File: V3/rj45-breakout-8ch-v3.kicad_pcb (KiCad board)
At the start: 2 copper layers, 93 x 67.8 mm, 13 parts, among them J1 Jack RJ45, J10 Conn_01x06, J11 Conn_01x06, J12 Conn_01x06, J13 Conn_01x06, J2 Jack RJ45, J3 Jack RJ45, J4 Jack RJ45, J5 Jack RJ45, J6 Jack RJ45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

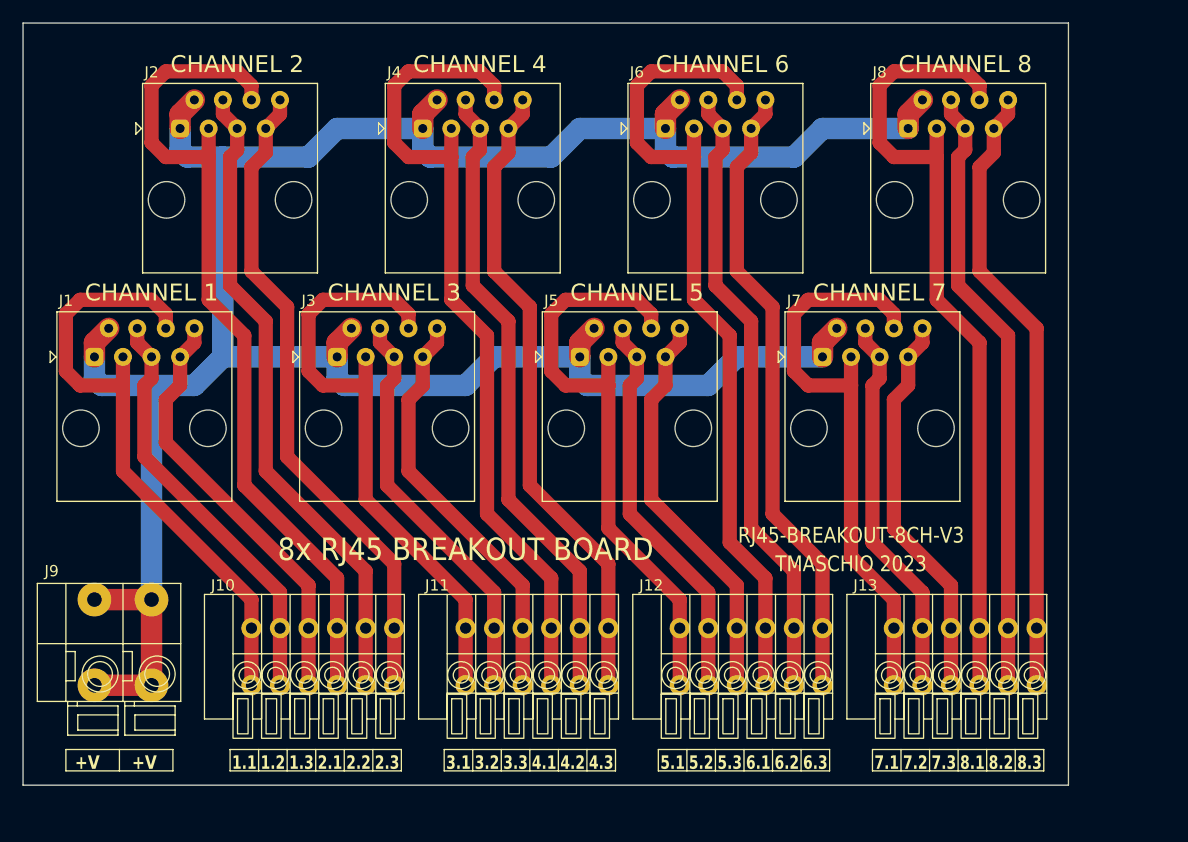
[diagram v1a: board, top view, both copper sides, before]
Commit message: Connectors rotated 180deg
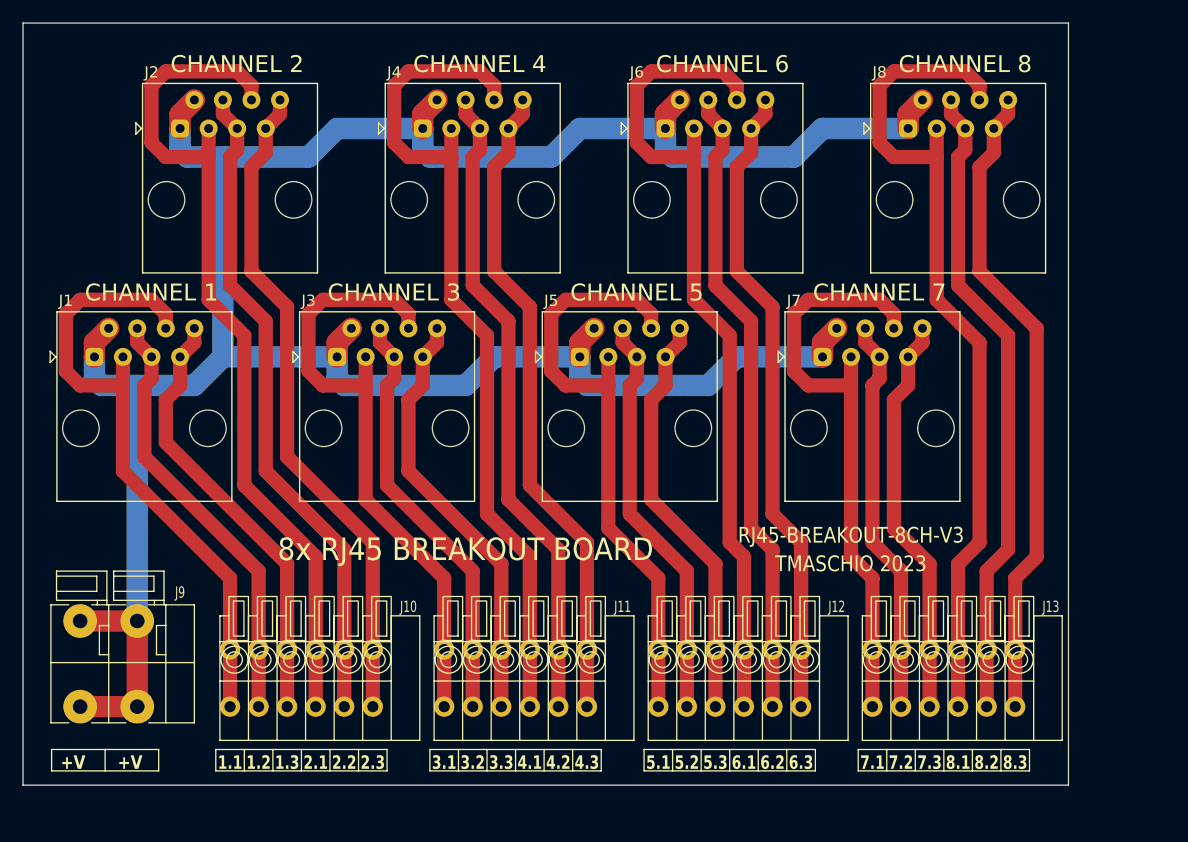
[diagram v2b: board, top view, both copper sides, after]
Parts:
- J10, J11, J12, J13: footprint Tales:TerminalBlock_DG141V-2.54-6P_1x06_P2.54mm_Vertical -> Tales:TerminalBlock_Phoenix_FFKDSA1-V-2.54-6_1x06_P2.54mm_Vertical
- J9: footprint Tales:TerminalBlock_JL142V-5.08-2P_1x02_P5.08mm_Vertical -> Tales:TerminalBlock_Phoenix_FFKDSA-V1-5.08-2_1x02_P5.08mm_Vertical
- moved J10 2.69 mm to (109.9, 120.0)
- moved J11 2.69 mm to (128.9, 120.0)
- moved J12 2.69 mm to (148.0, 120.0)
- moved J13 2.69 mm to (167.0, 120.0)
- moved J9 2.29 mm to (96.5, 120.0)
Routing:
- net Net-(J13-Pin_5): track 54.7 -> 57.4 mm
- net Net-(J13-Pin_4): track 73.0 -> 75.7 mm
- net Net-(J13-Pin_6): track 55.2 -> 57.9 mm
- net Net-(J9-Pin_1): track 228.0 -> 229.9 mm
- net Net-(J11-Pin_3): track 37.0 -> 38.1 mm
- net Net-(J10-Pin_4): track 76.2 -> 77.3 mm
- net Net-(J10-Pin_6): track 58.4 -> 59.5 mm
- net Net-(J13-Pin_3): track 34.9 -> 36.0 mm
- net Net-(J13-Pin_2): track 34.4 -> 35.5 mm
- net Net-(J12-Pin_6): track 56.3 -> 57.4 mm
- net Net-(J12-Pin_5): track 55.8 -> 56.9 mm
- net Net-(J12-Pin_4): track 74.1 -> 75.2 mm
- net Net-(J12-Pin_3): track 36.0 -> 37.1 mm
- net Net-(J12-Pin_1): track 53.7 -> 54.9 mm
- net Net-(J11-Pin_5): track 56.8 -> 57.9 mm
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
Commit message: Layout tweakings
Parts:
- added ?: , Tales:Grandmas_medium, F.Cu at (114.1, 103.8)
- J10: value Conn_01x06 -> SWITCHES1; footprint Tales:TerminalBlock_Phoenix_FFKDSA1-V-2.54-6_1x06_P2.54mm_Vertical -> Tales:TerminalBlock_DB141V-2.54-6P_1x06_P2.54mm_Vertical
- J11: value Conn_01x06 -> SWITCHES2; footprint Tales:TerminalBlock_Phoenix_FFKDSA1-V-2.54-6_1x06_P2.54mm_Vertical -> Tales:TerminalBlock_DB141V-2.54-6P_1x06_P2.54mm_Vertical
- J12: value Conn_01x06 -> SWITCHES3; footprint Tales:TerminalBlock_Phoenix_FFKDSA1-V-2.54-6_1x06_P2.54mm_Vertical -> Tales:TerminalBlock_DB141V-2.54-6P_1x06_P2.54mm_Vertical
- J13: value Conn_01x06 -> SWITCHES4; footprint Tales:TerminalBlock_Phoenix_FFKDSA1-V-2.54-6_1x06_P2.54mm_Vertical -> Tales:TerminalBlock_DB141V-2.54-6P_1x06_P2.54mm_Vertical
- J9: value Conn_01x02 -> 24V; footprint Tales:TerminalBlock_Phoenix_FFKDSA-V1-5.08-2_1x02_P5.08mm_Vertical -> Tales:TerminalBlock_DB142V-2-5.08_1x02_P5.08mm_Vertical
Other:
- board text added: "GHHA 2023"
- board text added: "Grandma's House"
- board text added: "Home Automation"
- board text removed: "8x RJ45 BREAKOUT BOARD"
- board text removed: "TMASCHIO 2023"

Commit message: Footprints updated
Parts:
- J1, J2, J3, J4, J5, J6, J7, J8: footprint Tales:RJ45_Amphenol_P-RJE08-188-0X10 -> Tales:RJ45_CKMTW_R-RJ45S08P-A004

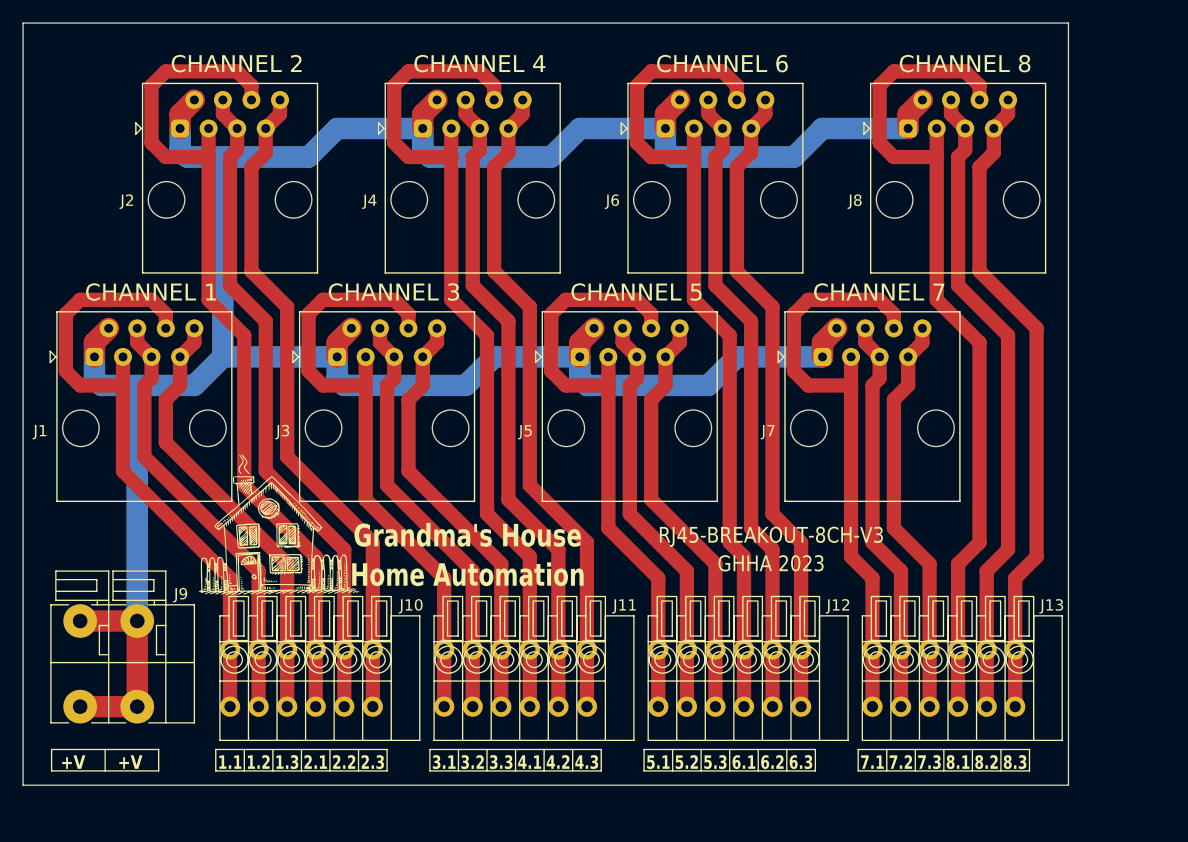
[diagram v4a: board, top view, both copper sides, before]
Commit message: Grid changed to mm
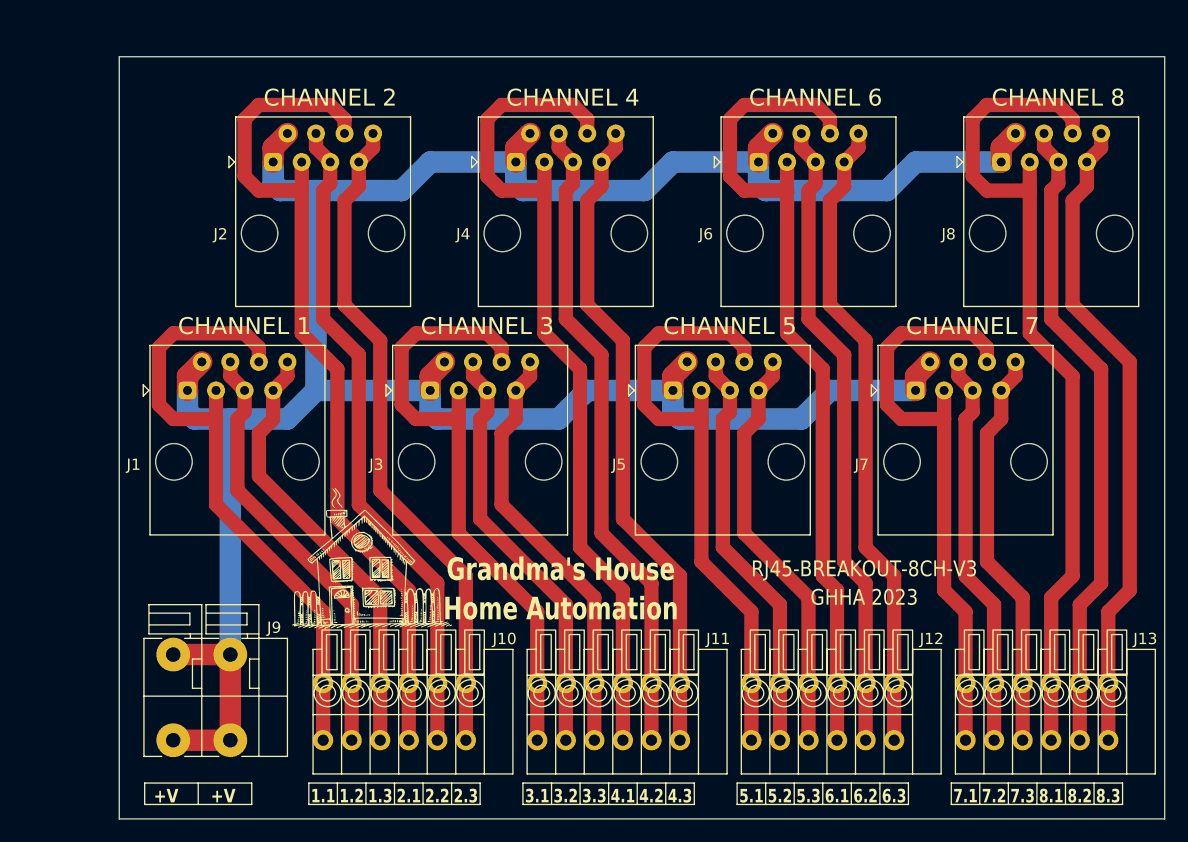
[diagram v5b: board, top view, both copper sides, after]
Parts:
- moved ? 8.80 mm to (122.4, 106.8)
- moved J1 8.80 mm to (110.5, 91.9)
- moved J10 8.80 mm to (118.1, 123.0)
- moved J11 8.80 mm to (137.2, 123.0)
- moved J12 8.80 mm to (156.2, 123.0)
- moved J13 8.80 mm to (175.3, 123.0)
- moved J2 8.80 mm to (118.1, 71.6)
- moved J4 8.80 mm to (139.7, 71.6)
- moved J5 8.80 mm to (153.7, 91.9)
- moved J6 8.80 mm to (161.3, 71.6)
- moved J7 8.80 mm to (175.3, 91.9)
- moved J8 8.80 mm to (182.9, 71.6)
- moved J9 8.80 mm to (104.8, 123.0)
- moved J3 8.80 mm to (132.1, 91.9)

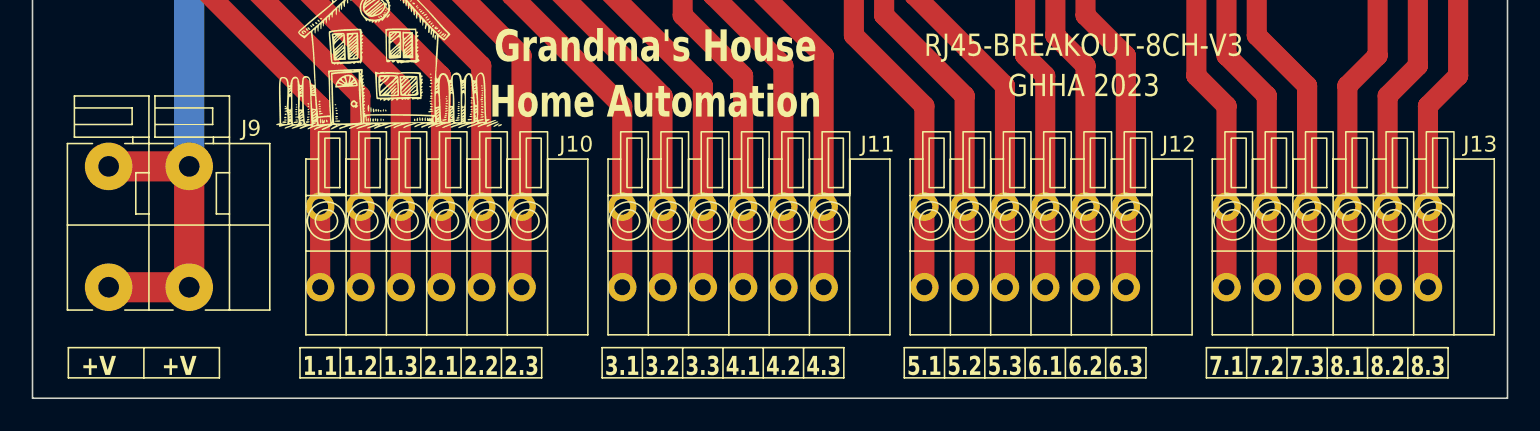
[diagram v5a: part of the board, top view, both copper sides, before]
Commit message: Align parts and tracks to mm grid
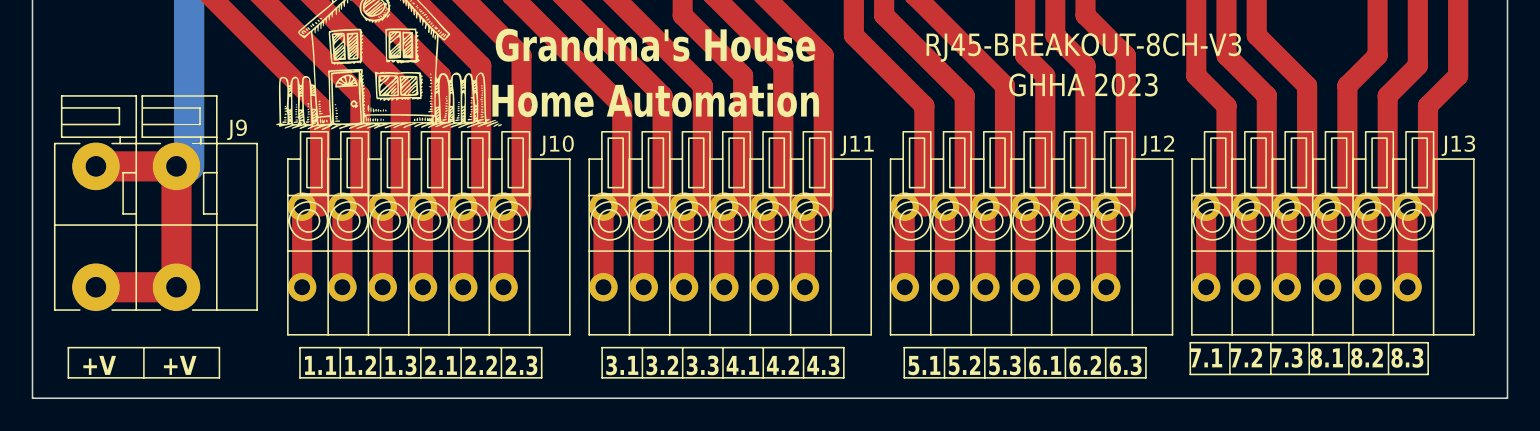
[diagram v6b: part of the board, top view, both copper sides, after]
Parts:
- moved J13 1.28 mm to (174.0, 123.0)
- moved J12 1.24 mm to (155.0, 123.0)
- moved J11 1.19 mm to (136.0, 123.0)
- moved J10 1.14 mm to (117.0, 123.0)
- moved J9 0.80 mm to (104.0, 123.0)

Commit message: Update rj45-breakout-8ch-v3.kicad_pcb
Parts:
- removed ?: , Tales:Grandmas_medium
- moved J7 0.36 mm to (174.9, 92.0)
- moved J2 0.32 mm to (118.4, 71.5)
- moved J5 0.28 mm to (153.4, 92.0)
- moved J4 0.23 mm to (139.9, 71.5)
- moved J3 0.20 mm to (131.9, 92.0)
- moved J6 0.15 mm to (161.4, 71.5)
- moved J1 0.13 mm to (110.4, 92.0)
- moved J8 0.08 mm to (182.9, 71.5)
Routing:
- net Net-(J12-Pin_2): track 36.5 -> 8.15 mm
- net Net-(J13-Pin_3): track 36.0 -> 8.15 mm
- net Net-(J13-Pin_2): track 35.5 -> 8.15 mm
- net Net-(J11-Pin_6): track 58.4 -> 38.2 mm
- net Net-(J13-Pin_6): track 57.9 -> 37.7 mm
- net Net-(J12-Pin_6): track 57.4 -> 38.2 mm
- net Net-(J11-Pin_5): track 57.9 -> 39.4 mm
- net Net-(J12-Pin_5): track 56.9 -> 39.4 mm
- net Net-(J11-Pin_4): track 76.2 -> 60.5 mm
- net Net-(J12-Pin_4): track 75.2 -> 60.5 mm
- net Net-(J12-Pin_3): track 37.1 -> 42.6 mm
- net Net-(J13-Pin_5): track 57.4 -> 55.6 mm
- net Net-(J9-Pin_1): track 229.9 -> 228.3 mm
- net Net-(J13-Pin_1): track 53.8 -> 55.4 mm
- net Net-(J13-Pin_4): track 75.7 -> 76.8 mm
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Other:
- board text removed: "Grandma's House"
- board text removed: "Home Automation"

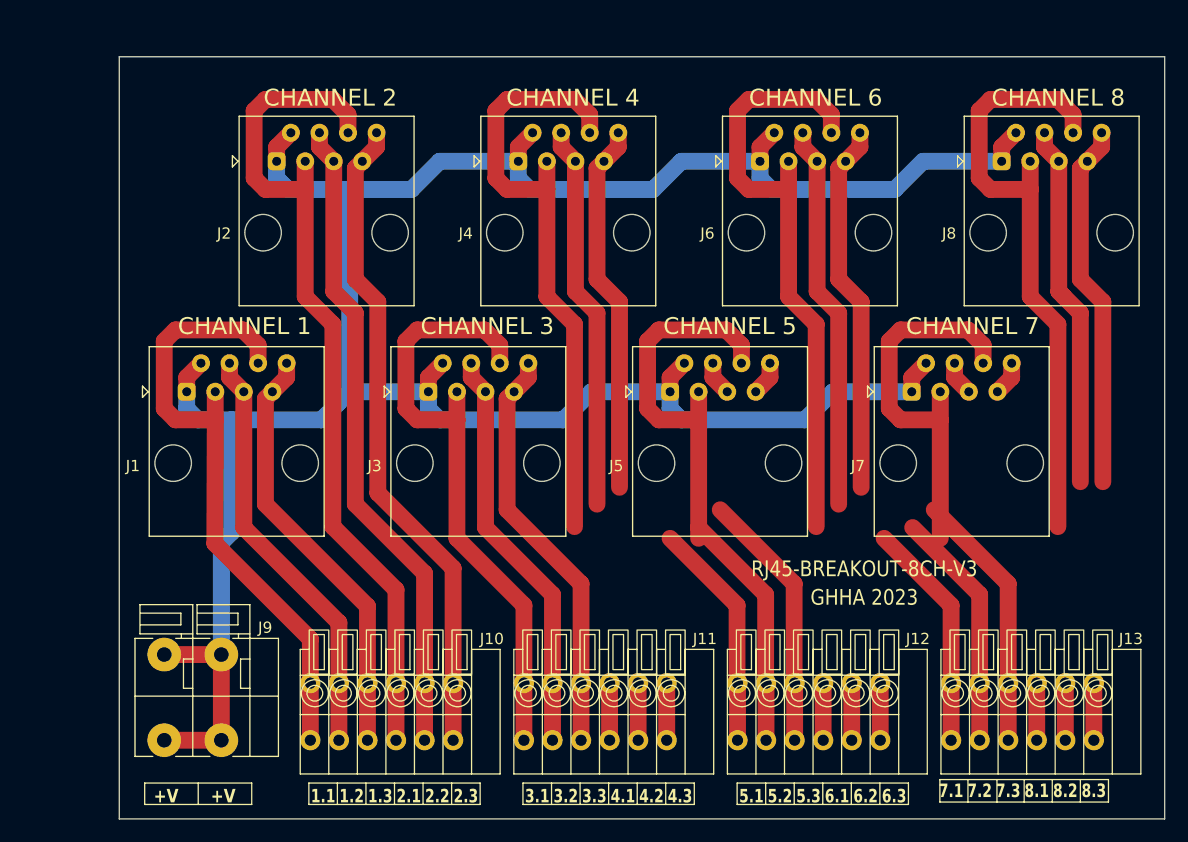
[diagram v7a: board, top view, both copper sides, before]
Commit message: Move to mm grid
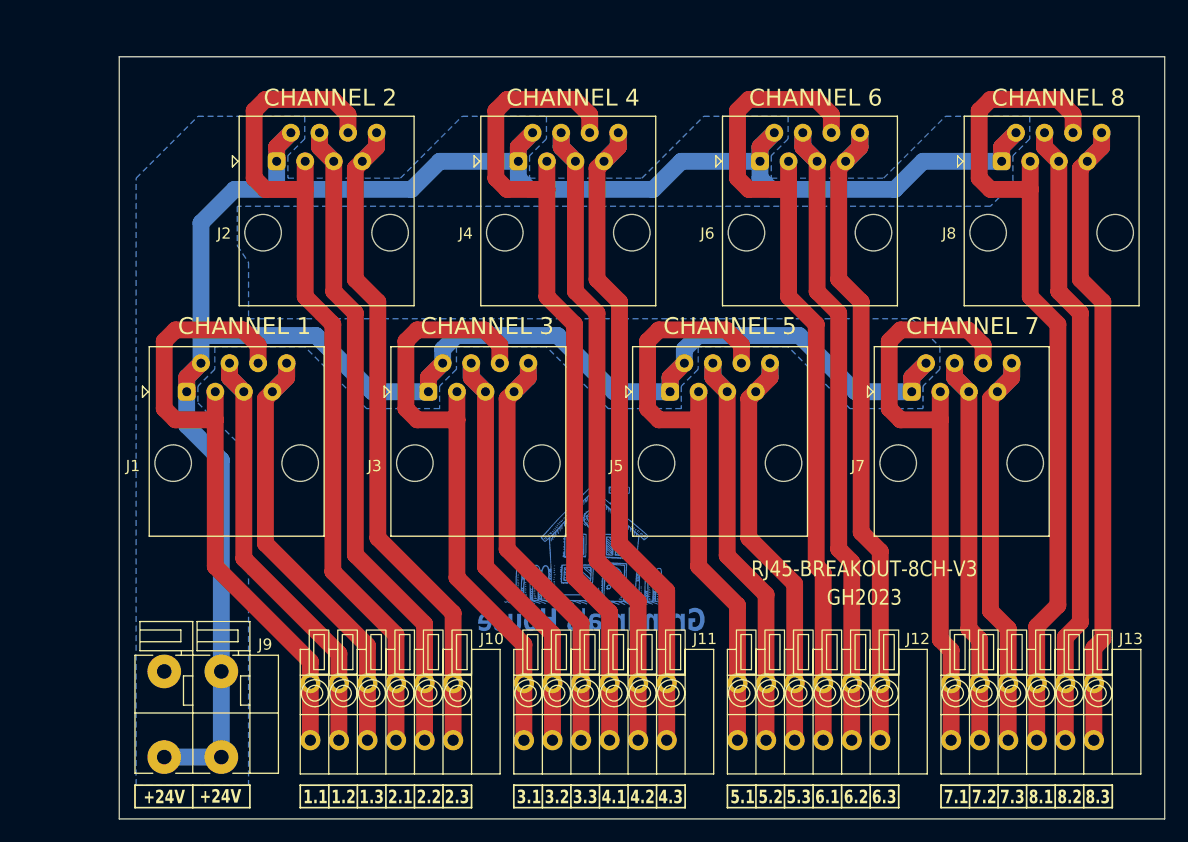
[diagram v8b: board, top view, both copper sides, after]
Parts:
- added Ref**: Val**, Tales:Grandmas_medium_bottom, F.Cu at (142.0, 111.0)
- moved J9 1.50 mm to (104.0, 124.5)
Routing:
- net Net-(J12-Pin_2): track 8.15 -> 38.6 mm
- net Net-(J13-Pin_3): track 8.15 -> 38.0 mm
- net Net-(J13-Pin_2): track 8.15 -> 37.5 mm
- net Net-(J9-Pin_1): track 228.3 -> 252.7 mm
- net Net-(J11-Pin_6): track 38.2 -> 60.5 mm
- net Net-(J13-Pin_6): track 37.7 -> 59.0 mm
- net Net-(J12-Pin_6): track 38.2 -> 59.4 mm
- net Net-(J11-Pin_5): track 39.4 -> 59.9 mm
- net Net-(J12-Pin_5): track 39.4 -> 58.9 mm
- net Net-(J11-Pin_4): track 60.5 -> 75.7 mm
- net Net-(J12-Pin_4): track 60.5 -> 74.7 mm
- net Net-(J12-Pin_3): track 42.6 -> 39.1 mm
- net Net-(J13-Pin_5): track 55.6 -> 59.0 mm
- net Net-(J11-Pin_2): track 36.5 -> 39.6 mm
- net Net-(J10-Pin_6): track 58.4 -> 61.5 mm
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- added copper zone on B.Cu, net Net-(J9-Pin_1)
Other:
- board text added: "+24V"
- board text added: "GH2023"
- board text added: "Grandma's House"
- board text removed: "+V"
- board text removed: "GHHA 2023"
